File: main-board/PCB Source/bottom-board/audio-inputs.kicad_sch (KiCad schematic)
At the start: 81 parts, among them P10 JACK_TRS_6PINS, P9 JACK_TRS_6PINS, Q1 2N7002, Q2 2N7002, Q3 MMBFJ110, Q4 MMBFJ110, Q5 MMBFJ110, Q6 MMBFJ110, Q7 2N7002, Q8 2N7002, U5 LM4562

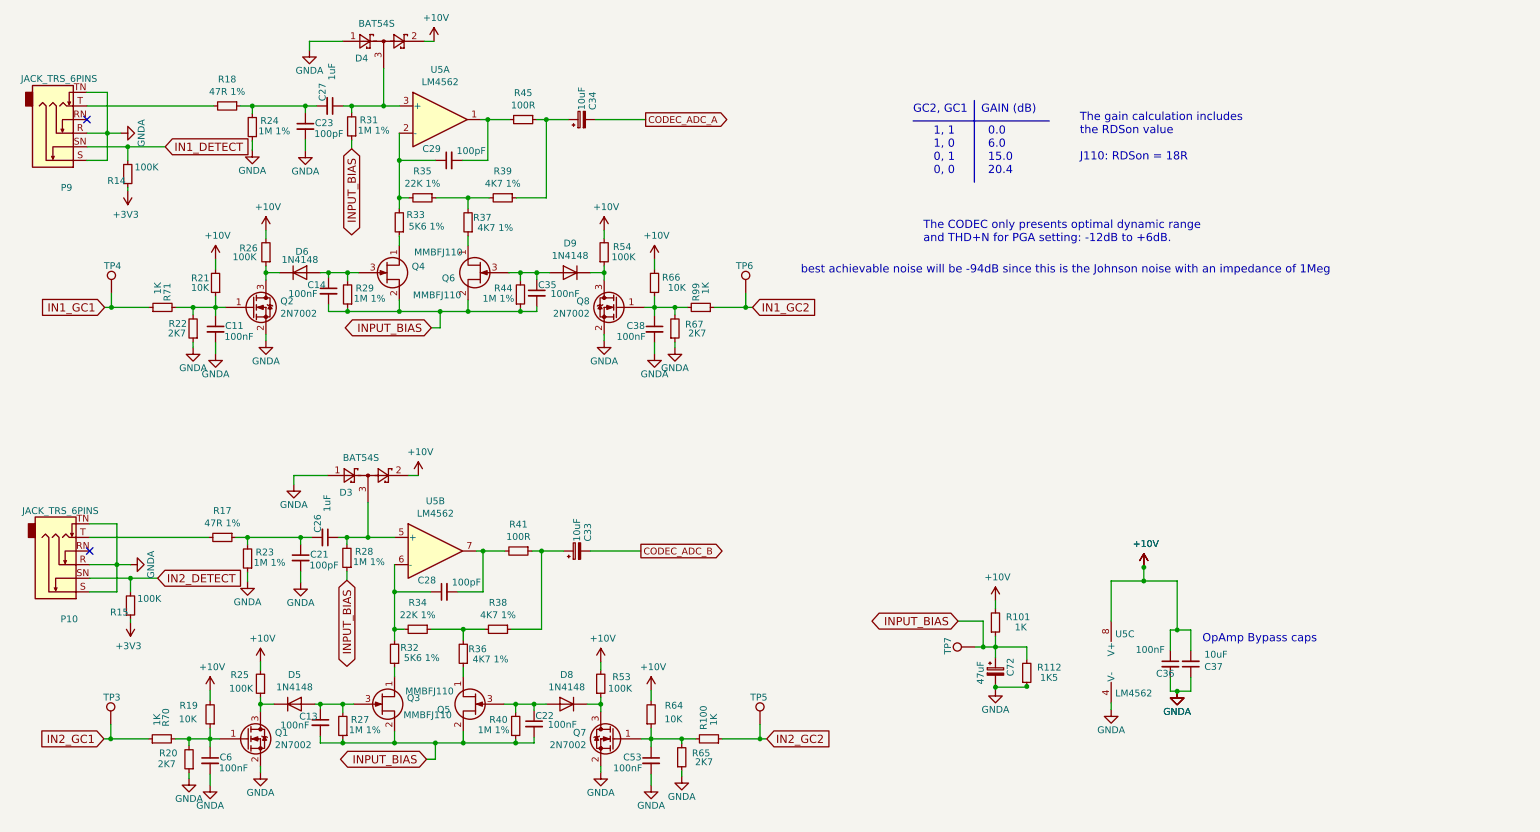
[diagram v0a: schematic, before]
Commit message: mainboard: add bias buffer, update MPNs, clean schematic
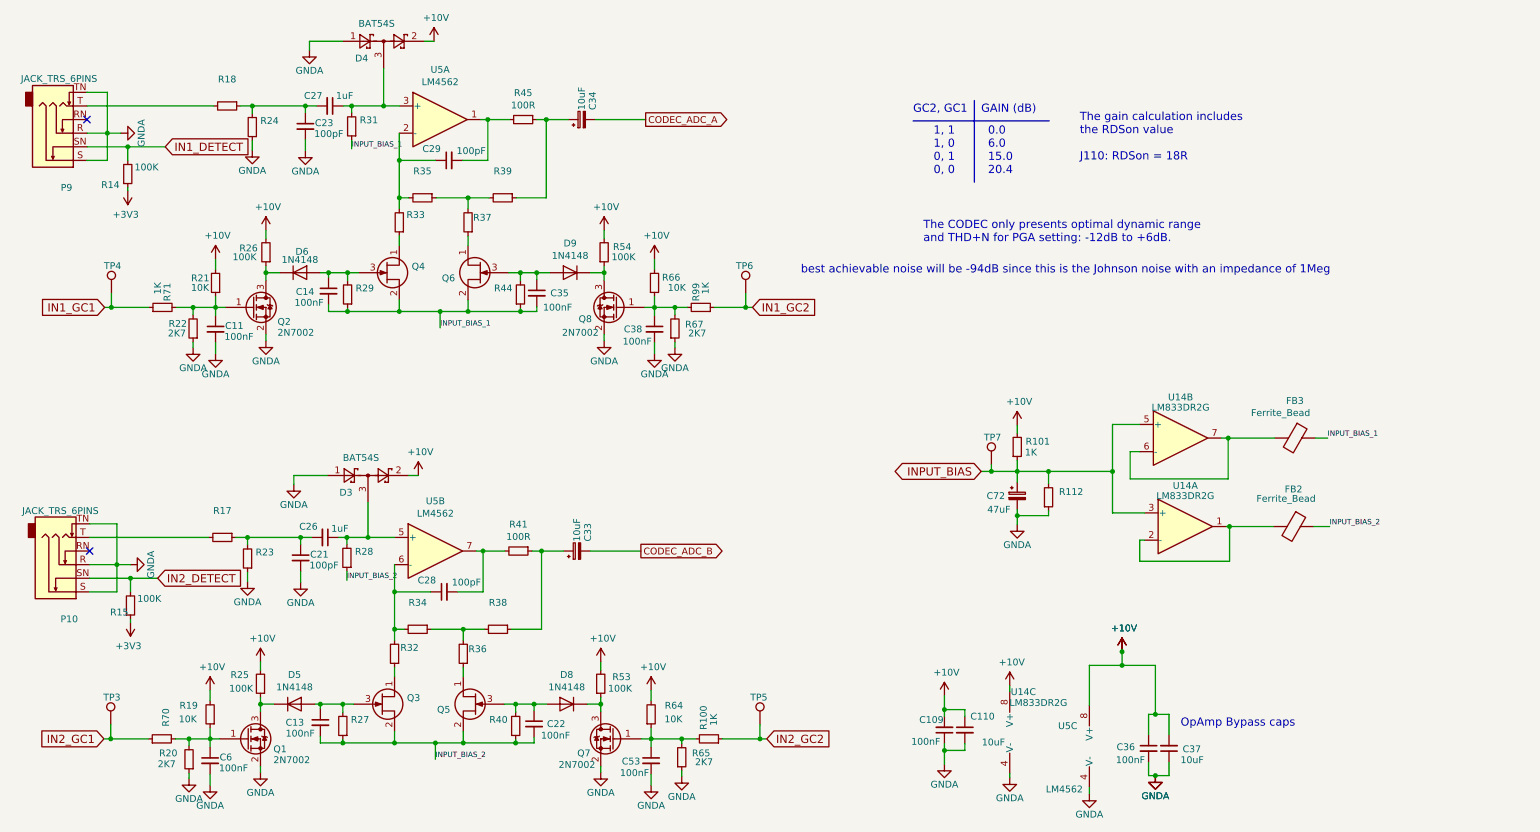
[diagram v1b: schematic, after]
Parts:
- added C109: 100nF, Capacitor_SMD:C_0603_1608Metric, symbol bottom-board-rescue:C_Small-Device
- added C110: 10uF, Capacitor_SMD:C_0805_2012Metric, symbol bottom-board-rescue:C_Small-Device
- added FB2, FB3: Ferrite_Bead, Resistor_SMD:R_0603_1608Metric, symbol Device:Ferrite_Bead
- added U14: LM833DR2G, Package_SO:SOIC-8_3.9x4.9mm_P1.27mm, symbol bottom-board-rescue:LM4562-Amplifier_Operational
- Q3, Q4, Q5, Q6: value MMBFJ110 -> (none); footprint Package_TO_SOT_SMD:SOT-23 -> (none); MPN MMBFJ110 -> MMBFJ211CT-ND
- R112: value 1K5 -> (none); footprint Resistor_SMD:R_0603_1608Metric -> (none); MPN (none) -> ERJ-PB3D1501V
- R17, R18: value 47R 1% -> (none); footprint Resistor_SMD:R_0603_1608Metric -> (none)
- R23, R24, R27, R28, R29, R31, R40, R44: value 1M 1% -> (none); footprint Resistor_SMD:R_0603_1608Metric -> (none)
- R32, R33: value 5K6 1% -> (none); footprint Resistor_SMD:R_0603_1608Metric -> (none)
- R34: value 22K 1% -> (none)
- R35: value 22K 1% -> (none); footprint Resistor_SMD:R_0603_1608Metric -> (none)
- R36: value 4K7 1% -> (none); footprint Resistor_SMD:R_0603_1608Metric -> (none)
- R37, R38, R39: value 4K7 1% -> (none)
- R70: value 1K -> (none); footprint Resistor_SMD:R_0603_1608Metric -> (none)
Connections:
- net +10V: now also C109.2, C110.1, U14.8 (V+)
- net GNDA: now also C109.1, C110.2, U14.4 (V-)
- net INPUT_BIAS: now also U14.3 (+), U14.5 (+); no longer C13.2, C14.2, C22.2, C35.2, Q3.2 (S), Q4.2 (S), Q5.2 (S), Q6.2 (S), R27.1, R28.1, R29.1, R31.1, R40.1, R44.1
- new net: FB2.2, U14.1, U14.2 (-)
- new net: FB3.2, U14.6 (-), U14.7
- new net INPUT_BIAS_1: C14.2, C35.2, FB3.1, Q4.2 (S), Q6.2 (S), R29.1, R31.1, R44.1
- new net INPUT_BIAS_2: C13.2, C22.2, FB2.1, Q3.2 (S), Q5.2 (S), R27.1, R28.1, R40.1
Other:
- moved on the sheet: C36, C37, C72, R101, R112, TP7, U5C

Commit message: mainboard: modify silkscreen
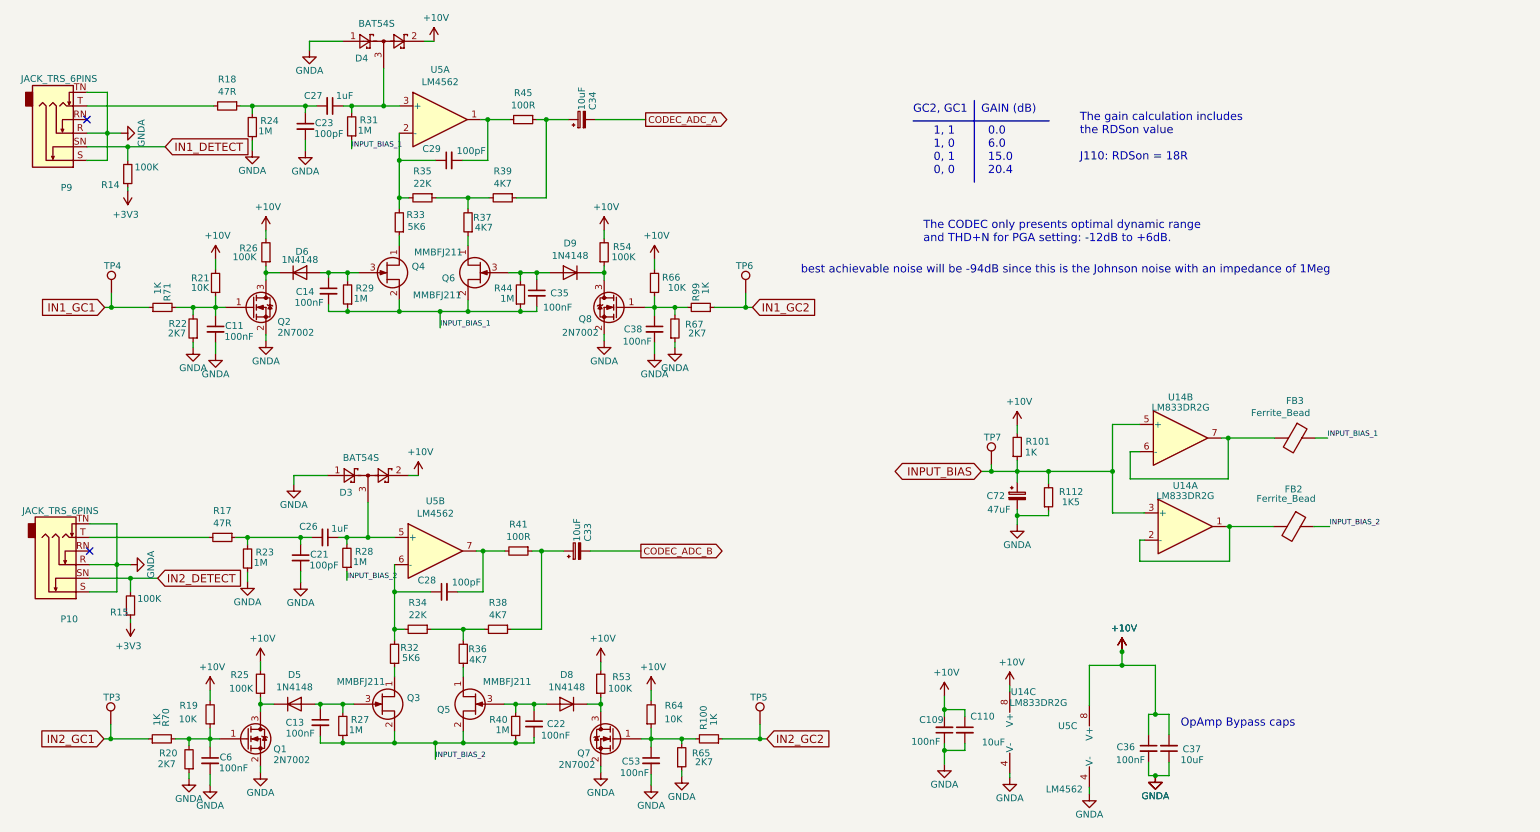
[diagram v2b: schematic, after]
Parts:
- Q3, Q4, Q5, Q6: value (none) -> MMBFJ211; footprint (none) -> Package_TO_SOT_SMD:SOT-23
- R112: value (none) -> 1K5; footprint (none) -> Resistor_SMD:R_0603_1608Metric
- R17, R18: value (none) -> 47R; footprint (none) -> Resistor_SMD:R_0603_1608Metric
- R23, R24, R27, R28, R29, R31, R40, R44: value (none) -> 1M; footprint (none) -> Resistor_SMD:R_0603_1608Metric
- R32, R33: value (none) -> 5K6; footprint (none) -> Resistor_SMD:R_0603_1608Metric
- R34: value (none) -> 22K
- R35: value (none) -> 22K; footprint (none) -> Resistor_SMD:R_0603_1608Metric
- R36: value (none) -> 4K7; footprint (none) -> Resistor_SMD:R_0603_1608Metric
- R37, R38, R39: value (none) -> 4K7
- R70: value (none) -> 1K; footprint (none) -> Resistor_SMD:R_0603_1608Metric
